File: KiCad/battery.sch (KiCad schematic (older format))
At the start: 7 parts, among them J1 Conn_01x07_Male, J2 Conn_01x01_Male, J3 Conn_01x01_Male, U1 ATtiny85-20SU, U2 LD1117S33TR_SOT223

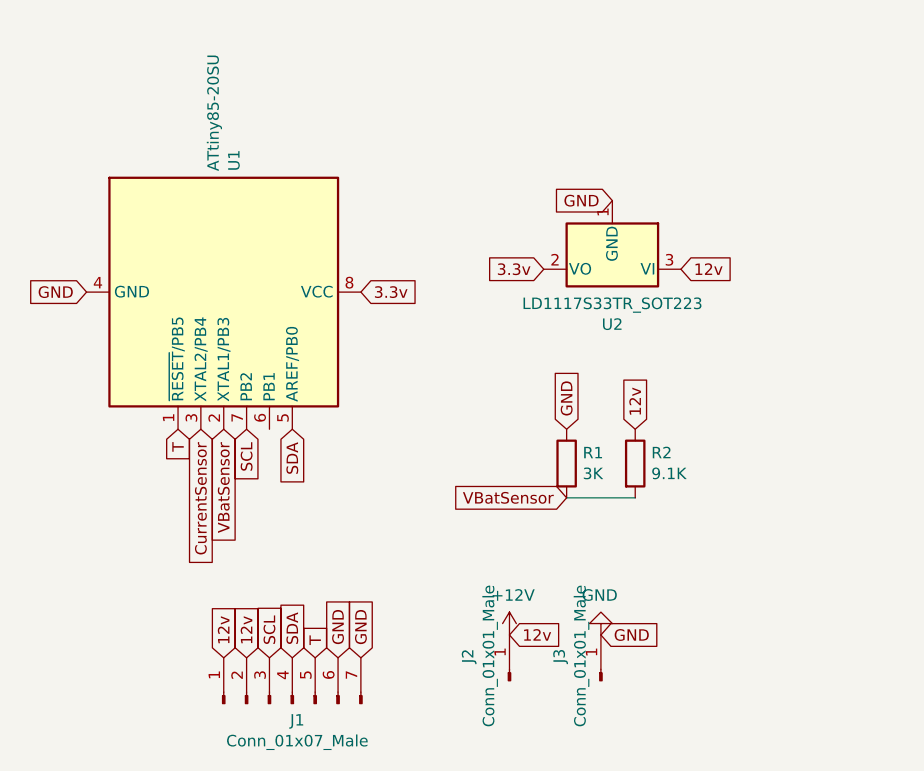
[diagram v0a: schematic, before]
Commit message: Use PB4 to pull T pin low instead of PB5
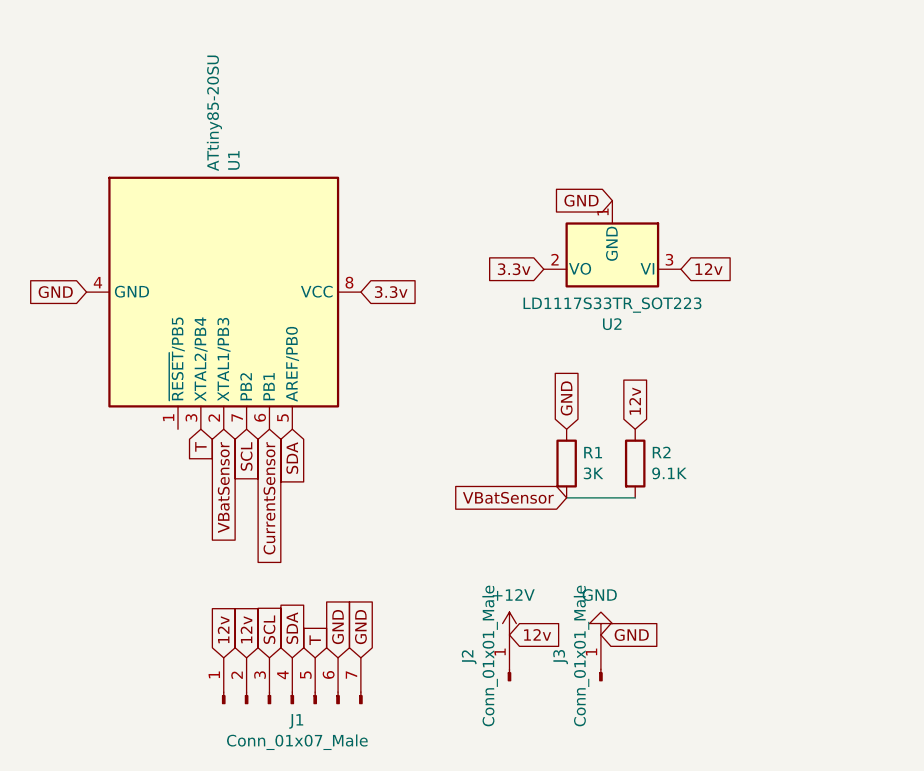
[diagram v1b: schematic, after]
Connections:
- net CurrentSensor: now also U1.6 (PB1); no longer U1.3 (XTAL2/PB4)
- net T: now also U1.3 (XTAL2/PB4); no longer U1.1 (~RESET~/PB5)
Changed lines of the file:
@@
 Text GLabel 3400 1750 2    50   Input ~ 0
 3.3v
-Text GLabel 2700 2350 3    50   Input ~ 0
+Text GLabel 3000 2350 3    50   Input ~ 0
 CurrentSensor
 $Comp
@@
 	0    1    1    0
 $EndComp
-Text GLabel 2600 2350 3    50   Input ~ 0
+Text GLabel 2700 2350 3    50   Input ~ 0
 T
 Text GLabel 2900 2350 3    50   Input ~ 0

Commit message: Update PCB before manufacturing
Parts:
- removed J1: Conn_01x07_Male, Connector_PinHeader_2.54mm:PinHeader_1x07_P2.54mm_Vertical, symbol Connector:Conn_01x07_Male
- removed J2, J3: Conn_01x01_Male, Connector_Pin:Pin_D1.4mm_L8.5mm_W2.8mm_FlatFork, symbol Connector:Conn_01x01_Male
- added C1, C2: 22uF, Capacitor_SMD:C_0805_2012Metric, symbol Device:R
- added J1: Conn_01x06_Male, Connector_PinHeader_2.54mm:PinHeader_1x06_P2.54mm_Horizontal, symbol Connector:Conn_01x06_Male
- added J2: Conn_01x02_Male, Connector_PinHeader_2.54mm:PinHeader_1x02_P2.54mm_Vertical, symbol Connector:Conn_01x02_Male
- added R3, R4: 10k, Resistor_SMD:R_0402_1005Metric, symbol Device:R
- R1: value 3K -> 3.3K; footprint Parts:R_1206_3216Metric_Pad1.42x1.75mm_HandSolder -> Resistor_SMD:R_0402_1005Metric
- R2: value 9.1K -> 10K; footprint Parts:R_1206_3216Metric_Pad1.42x1.75mm_HandSolder -> Resistor_SMD:R_0402_1005Metric
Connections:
- net 3.3v: now also C1.1, J2.1 (Pin_1), R4.1
- net CurrentSensor: now also J1.5 (Pin_5)
- net GND: now also C1.2, C2.2, J1.6 (Pin_6), J2.2 (Pin_2)
- net SCL: now also J1.3 (Pin_3)
- net SDA: now also J1.2 (Pin_2)
- net T: now also J1.4 (Pin_4), R3.2; no longer U1.3 (XTAL2/PB4)
- net R: now reaches U1.1 (~RESET~/PB5)
- net R: now also R4.2
- net +12V renamed 12v
- net 12v: now also C2.1, J1.1 (Pin_1)
- new net T_C: R3.1, U1.3 (XTAL2/PB4)
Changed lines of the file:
@@
 EESchema Schematic File Version 4
-LIBS:battery-cache
-EELAYER 26 0
+EELAYER 30 0
 EELAYER END
 $Descr A4 11693 8268
@@
 P 4600 2500
 F 0 "R2" H 4670 2546 50  0000 L CNN
-F 1 "9.1K" H 4670 2455 50  0000 L CNN
-F 2 "Parts:R_1206_3216Metric_Pad1.42x1.75mm_HandSolder" V 4530 2500 50  0001 C CNN
+F 1 "10K" H 4670 2455 50  0000 L CNN
+F 2 "Resistor_SMD:R_0402_1005Metric" V 4530 2500 50  0001 C CNN
 F 3 "~" H 4600 2500 50  0001 C CNN
 	1    4600 2500
@@
 P 4300 2500
 F 0 "R1" H 4370 2546 50  0000 L CNN
-F 1 "3K" H 4370 2455 50  0000 L CNN
-F 2 "Parts:R_1206_3216Metric_Pad1.42x1.75mm_HandSolder" V 4230 2500 50  0001 C CNN
+F 1 "3.3K" H 4370 2455 50  0000 L CNN
+F 2 "Resistor_SMD:R_0402_1005Metric" V 4230 2500 50  0001 C CNN
 F 3 "~" H 4300 2500 50  0001 C CNN
 	1    4300 2500
 	1    0    0    -1
 $EndComp
-$Comp
-L power:GND #PWR0101
-U 1 1 5EC353CA
-P 4450 3250
-F 0 "#PWR0101" H 4450 3000 50  0001 C CNN
-F 1 "GND" H 4455 3077 50  0000 C CNN
-F 2 "" H 4450 3250 50  0001 C CNN
-F 3 "" H 4450 3250 50  0001 C CNN
-	1    4450 3250
-	-1   0    0    1
-$EndComp
-$Comp
-L Connector:Conn_01x07_Male J1
-U 1 1 5EC62E55
-P 3100 3550
-F 0 "J1" V 3027 3528 50  0000 C CNN
-F 1 "Conn_01x07_Male" V 2936 3528 50  0000 C CNN
-F 2 "Connector_PinHeader_2.54mm:PinHeader_1x07_P2.54mm_Vertical" H 3100 3550 50  0001 C CNN
-F 3 "~" H 3100 3550 50  0001 C CNN
-	1    3100 3550
-	0    -1   -1   0
-$EndComp
-Text GLabel 2800 3350 1    50   Input ~ 0
+Text GLabel 3900 3450 1    50   Input ~ 0
 12v
-Text GLabel 2900 3350 1    50   Input ~ 0
-12v
-Text GLabel 3000 3350 1    50   Input ~ 0
-SCL
-Text GLabel 3100 3350 1    50   Input ~ 0
-SDA
-Text GLabel 3200 3350 1    50   Input ~ 0
-T
-Text GLabel 3300 3350 1    50   Input ~ 0
-GND
-Text GLabel 3400 3350 1    50   Input ~ 0
+Text GLabel 4400 3450 1    50   Input ~ 0
 GND
 $Comp
@@
 	-1   0    0    1
 $EndComp
-$Comp
-L power:+12V #PWR0102
-U 1 1 5EC34276
-P 4050 3250
-F 0 "#PWR0102" H 4050 3100 50  0001 C CNN
-F 1 "+12V" H 4065 3423 50  0000 C CNN
-F 2 "" H 4050 3250 50  0001 C CNN
-F 3 "" H 4050 3250 50  0001 C CNN
-	1    4050 3250
-	1    0    0    -1
-$EndComp
-Text GLabel 4050 3250 2    50   Input ~ 0
-12v
-Text GLabel 4450 3250 2    50   Input ~ 0
-GND
 Text GLabel 4800 1650 2    50   Input ~ 0
 12v
@@
 $EndComp
 Text GLabel 2700 2350 3    50   Input ~ 0
-T
+T_C
 Text GLabel 2900 2350 3    50   Input ~ 0
 SCL
@@
 SDA
 $Comp
-L Connector:Conn_01x01_Male J2
-U 1 1 5ECDB575
-P 4050 3450
-F 0 "J2" H 4158 3631 50  0000 C CNN
-F 1 "Conn_01x01_Male" H 4158 3540 50  0000 C CNN
-F 2 "Connector_Pin:Pin_D1.4mm_L8.5mm_W2.8mm_FlatFork" H 4050 3450 50  0001 C CNN
-F 3 "~" H 4050 3450 50  0001 C CNN
-	1    4050 3450
+L Device:R R4
+U 1 1 5F803F9D
+P 5300 2500
+F 0 "R4" H 5370 2546 50  0000 L CNN
+F 1 "10k" H 5370 2455 50  0000 L CNN
+F 2 "Resistor_SMD:R_0402_1005Metric" V 5230 2500 50  0001 C CNN
+F 3 "~" H 5300 2500 50  0001 C CNN
+	1    5300 2500
+	1    0    0    -1
+$EndComp
+Text GLabel 2600 2350 3    50   Input ~ 0
+R
+Text GLabel 5300 2650 3    50   Input ~ 0
+R
+Text GLabel 5300 2350 1    50   Input ~ 0
+3.3v
+$Comp
+L Device:R C1
+U 1 1 5F8051D0
+P 3700 2250
+F 0 "C1" H 3770 2296 50  0000 L CNN
+F 1 "22uF" H 3770 2205 50  0000 L CNN
+F 2 "Capacitor_SMD:C_0805_2012Metric" V 3630 2250 50  0001 C CNN
+F 3 "~" H 3700 2250 50  0001 C CNN
+	1    3700 2250
+	1    0    0    -1
+$EndComp
+Text GLabel 3700 2100 1    50   Input ~ 0
+3.3v
+Text GLabel 3700 2400 3    50   Input ~ 0
+GND
+Text GLabel 4200 3450 1    50   Input ~ 0
+T
+$Comp
+L Device:R R3
+U 1 1 5F813E79
+P 4950 2950
+F 0 "R3" H 5020 2996 50  0000 L CNN
+F 1 "10k" H 5020 2905 50  0000 L CNN
+F 2 "Resistor_SMD:R_0402_1005Metric" V 4880 2950 50  0001 C CNN
+F 3 "~" H 4950 2950 50  0001 C CNN
+	1    4950 2950
+	1    0    0    -1
+$EndComp
+Text GLabel 4950 3100 3    50   Input ~ 0
+T
+Text GLabel 4950 2800 1    50   Input ~ 0
+T_C
+$Comp
+L Connector:Conn_01x06_Male J1
+U 1 1 5F8168A9
+P 4100 3650
+F 0 "J1" V 4254 3262 50  0000 R CNN
+F 1 "Conn_01x06_Male" V 4163 3262 50  0000 R CNN
+F 2 "Connector_PinHeader_2.54mm:PinHeader_1x06_P2.54mm_Horizontal" H 4100 3650 50  0001 C CNN
+F 3 "~" H 4100 3650 50  0001 C CNN
+	1    4100 3650
 	0    -1   -1   0
 $EndComp
+Text GLabel 4300 3450 1    50   Input ~ 0
+CurrentSensor
+Text GLabel 4100 3450 1    50   Input ~ 0
+SCL
+Text GLabel 4000 3450 1    50   Input ~ 0
+SDA
 $Comp
-L Connector:Conn_01x01_Male J3
-U 1 1 5ECDC6DD
-P 4450 3450
-F 0 "J3" H 4558 3631 50  0000 C CNN
-F 1 "Conn_01x01_Male" H 4558 3540 50  0000 C CNN
-F 2 "Connector_Pin:Pin_D1.4mm_L8.5mm_W2.8mm_FlatFork" H 4450 3450 50  0001 C CNN
-F 3 "~" H 4450 3450 50  0001 C CNN
-	1    4450 3450
+L Device:R C2
+U 1 1 5F823DED
+P 5500 1650
+F 0 "C2" H 5570 1696 50  0000 L CNN
+F 1 "22uF" H 5570 1605 50  0000 L CNN
+F 2 "Capacitor_SMD:C_0805_2012Metric" V 5430 1650 50  0001 C CNN
+F 3 "~" H 5500 1650 50  0001 C CNN
+	1    5500 1650
+	1    0    0    -1
+$EndComp
+Text GLabel 5500 1500 1    50   Input ~ 0
+12v
+Text GLabel 5500 1800 3    50   Input ~ 0
+GND
+$Comp
+L Connector:Conn_01x02_Male J2
+U 1 1 5F81605B
+P 3000 3700
+F 0 "J2" V 3154 3512 50  0000 R CNN
+F 1 "Conn_01x02_Male" V 3063 3512 50  0000 R CNN
+F 2 "Connector_PinHeader_2.54mm:PinHeader_1x02_P2.54mm_Vertical" H 3000 3700 50  0001 C CNN
+F 3 "~" H 3000 3700 50  0001 C CNN
+	1    3000 3700
 	0    -1   -1   0
 $EndComp
+Text GLabel 3000 3500 1    50   Input ~ 0
+3.3v
+Text GLabel 3100 3500 1    50   Input ~ 0
+GND
 $EndSCHEMATC
